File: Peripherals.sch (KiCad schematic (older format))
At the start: 18 parts, among them J2 5-5530843-4, J3 5-5530843-4, J4 5-5530843-4, J5 5-5530843-4, U6 CD74AC238, U7 74AHC138

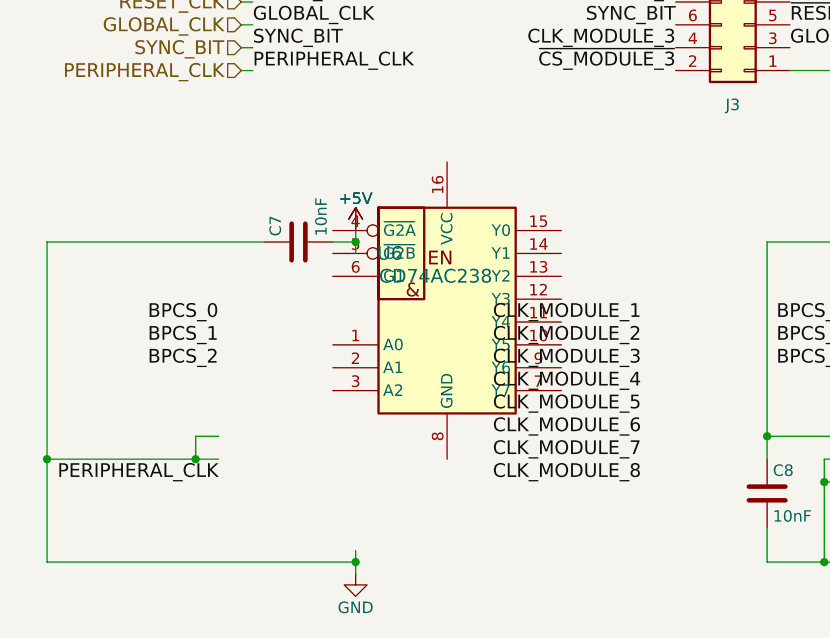
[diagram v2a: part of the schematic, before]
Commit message: Multiple change : Replacing old custom "LTC6994-1" symbol with the Kicad symbol "LTC6994xS6-1" Replacing old custom "LM810" symbol with the Kicad symbol "LM810" Replacing all hidden power pins symbols (hidden pins bug) Renaming "Main connector" to "SPS1 Processor connector" Removing old symbols, cleaning Replacing symbol "CD74AC238" with a new one
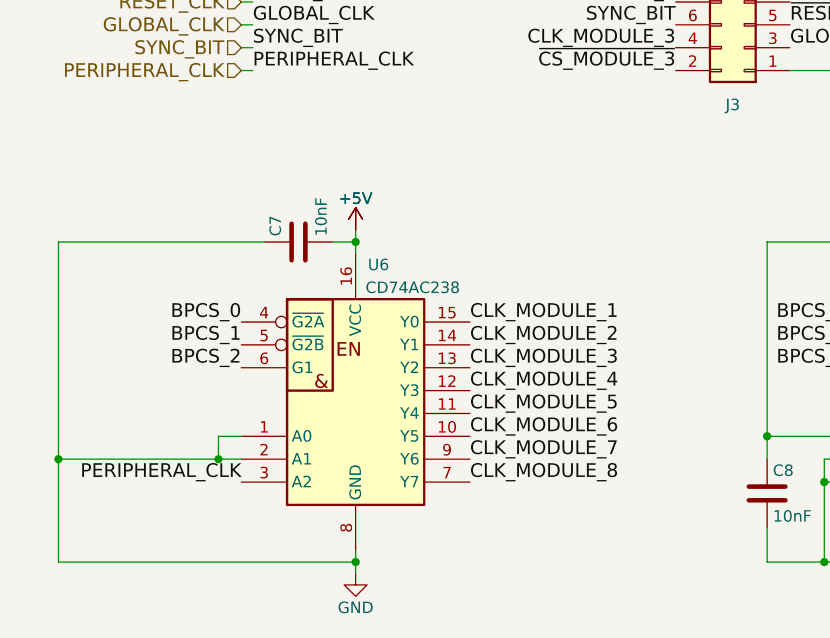
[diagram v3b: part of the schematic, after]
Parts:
- U6: footprint Package_SO:SOIC-16_3.9x9.9mm_P1.27mm -> (none)
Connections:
- net +5V: now also U6.16 (VCC)
- net BPCS_0: now also U6.4 (~G2A)
- net BPCS_1: now also U6.5 (~G2B)
- net BPCS_2: now also U6.6 (G1)
- net CLK_MODULE_1: now also U6.15 (Y0)
- net CLK_MODULE_2: now also U6.14 (Y1)
- net CLK_MODULE_3: now also U6.13 (Y2)
- net CLK_MODULE_4: now also U6.12 (Y3)
- net CLK_MODULE_5: now also U6.11 (Y4)
- net CLK_MODULE_6: now also U6.10 (Y5)
- net CLK_MODULE_7: now also U6.9 (Y6)
- net CLK_MODULE_8: now also U6.7 (Y7)
- net GND: now also U6.1 (A0), U6.2 (A1), U6.8 (GND)
- net PERIPHERAL_CLK: now also U6.3 (A2)
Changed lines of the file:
@@
 Text HLabel 1550 5100 0    60   Input ~ 0
 GLOBAL_CLK
-Text Label 2650 6400 0    60   ~ 0
+Text Label 2550 6400 0    60   ~ 0
 CLK_MODULE_1
-Text Label 2650 6500 0    60   ~ 0
+Text Label 2550 6500 0    60   ~ 0
 CLK_MODULE_2
-Text Label 2650 6600 0    60   ~ 0
+Text Label 2550 6600 0    60   ~ 0
 CLK_MODULE_3
-Text Label 2650 6700 0    60   ~ 0
+Text Label 2550 6700 0    60   ~ 0
 CLK_MODULE_4
 $Comp
@@
 Wire Wire Line
 	2050 6000 2050 6050
-Connection ~ 1350 7000
-Wire Wire Line
-	1350 6900 1350 7000
-Wire Wire Line
-	1450 6900 1350 6900
+Connection ~ 1450 7000
+Wire Wire Line
+	1450 6900 1450 7000
+Wire Wire Line
+	1550 6900 1450 6900
 Connection ~ 2050 7450
 Wire Wire Line
@@
 	1    0    0    -1
 $EndComp
-Text Label 1450 6400 2    60   ~ 0
+Text Label 1550 6400 2    60   ~ 0
 BPCS_0
-Text Label 1450 6500 2    60   ~ 0
+Text Label 1550 6500 2    60   ~ 0
 BPCS_1
 Wire Wire Line
@@
 Wire Wire Line
 	1550 5300 1600 5300
-Text Label 1450 6600 2    60   ~ 0
+Text Label 1550 6600 2    60   ~ 0
 BPCS_2
-Text Label 2650 6800 0    60   ~ 0
+Text Label 2550 6800 0    60   ~ 0
 CLK_MODULE_5
-Text Label 2650 6900 0    60   ~ 0
+Text Label 2550 6900 0    60   ~ 0
 CLK_MODULE_6
-Text Label 2650 7000 0    60   ~ 0
+Text Label 2550 7000 0    60   ~ 0
 CLK_MODULE_7
-Text Label 2650 7100 0    60   ~ 0
+Text Label 2550 7100 0    60   ~ 0
 CLK_MODULE_8
 Text HLabel 8800 5450 2    60   Output ~ 0
@@
 	2050 6050 2050 6100
 Wire Wire Line
-	1350 7000 1450 7000
+	1450 7000 1550 7000
 Wire Wire Line
 	2050 7450 2050 7500
@@
 $EndComp
 $Comp
-L Custom:CD74AC238 U6
-U 1 1 5D4D885E
-P 2450 6300
-F 0 "U6" H 2200 6500 60  0000 C CNN
-F 1 "CD74AC238" H 2400 6400 60  0000 C CNN
-F 2 "Package_SO:SOIC-16_3.9x9.9mm_P1.27mm" H 2450 6300 60  0001 C CNN
-F 3 "" H 2450 6300 60  0001 C CNN
-	1    2450 6300
-	1    0    0    -1
-$EndComp
-$Comp
 L 74xx:74LS138 U7
 U 1 1 5D4DDE08
@@
 Text Label 1600 5300 0    60   ~ 0
 PERIPHERAL_CLK
-Text Label 1450 7100 2    60   ~ 0
+Text Label 1550 7100 2    60   ~ 0
 PERIPHERAL_CLK
-Wire Wire Line
-	700  7450 700  7000
-Wire Wire Line
-	700  7450 2050 7450
-Wire Wire Line
-	700  6050 1650 6050
-Wire Wire Line
-	700  7000 1350 7000
-Connection ~ 700  7000
-Wire Wire Line
-	700  7000 700  6050
 $Comp
 L power:GND #PWR?
@@
 	4700 7500 4700 7450
 Connection ~ 4700 7450
+$Comp
+L Custom:CD74AC238 U6
+U 1 1 5F9BBC7E
+P 2050 6700
+F 0 "U6" H 2150 7250 50  0000 C CNN
+F 1 "CD74AC238" H 2300 7150 50  0000 C CNN
+F 2 "" H 2050 6800 50  0001 C CNN
+F 3 "" H 2050 6800 50  0001 C CNN
+	1    2050 6700
+	1    0    0    -1
+$EndComp
+Wire Wire Line
+	750  7000 750  7450
+Wire Wire Line
+	750  7000 1450 7000
+Wire Wire Line
+	750  7450 2050 7450
+Wire Wire Line
+	750  7000 750  6050
+Connection ~ 750  7000
+Wire Wire Line
+	750  6050 1650 6050
 Wire Bus Line
 	1600 3800 1600 4400
